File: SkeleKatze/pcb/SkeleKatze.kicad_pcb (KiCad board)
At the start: 2 copper layers, 54.5 x 82.9 mm, 6 parts, among them SW2 SW_Push

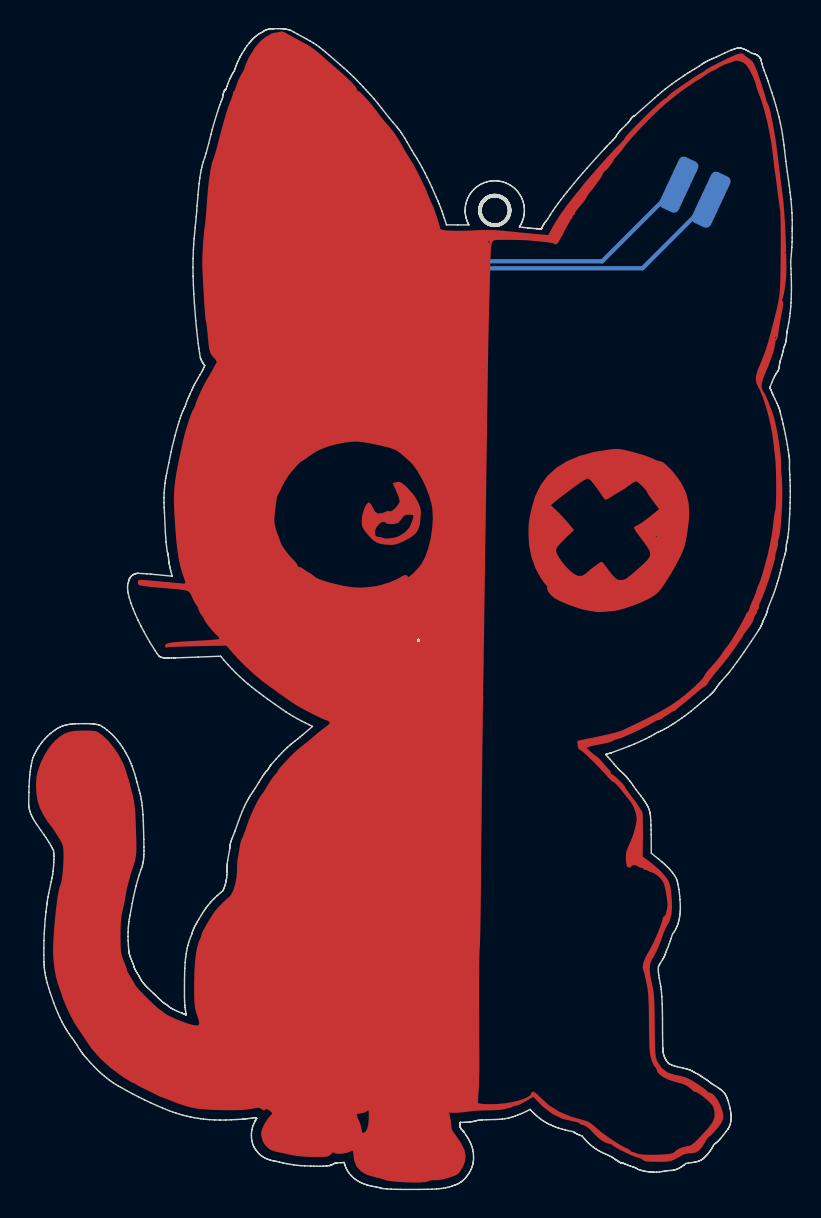
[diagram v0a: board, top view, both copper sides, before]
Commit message: Updated base image to fix mask issues
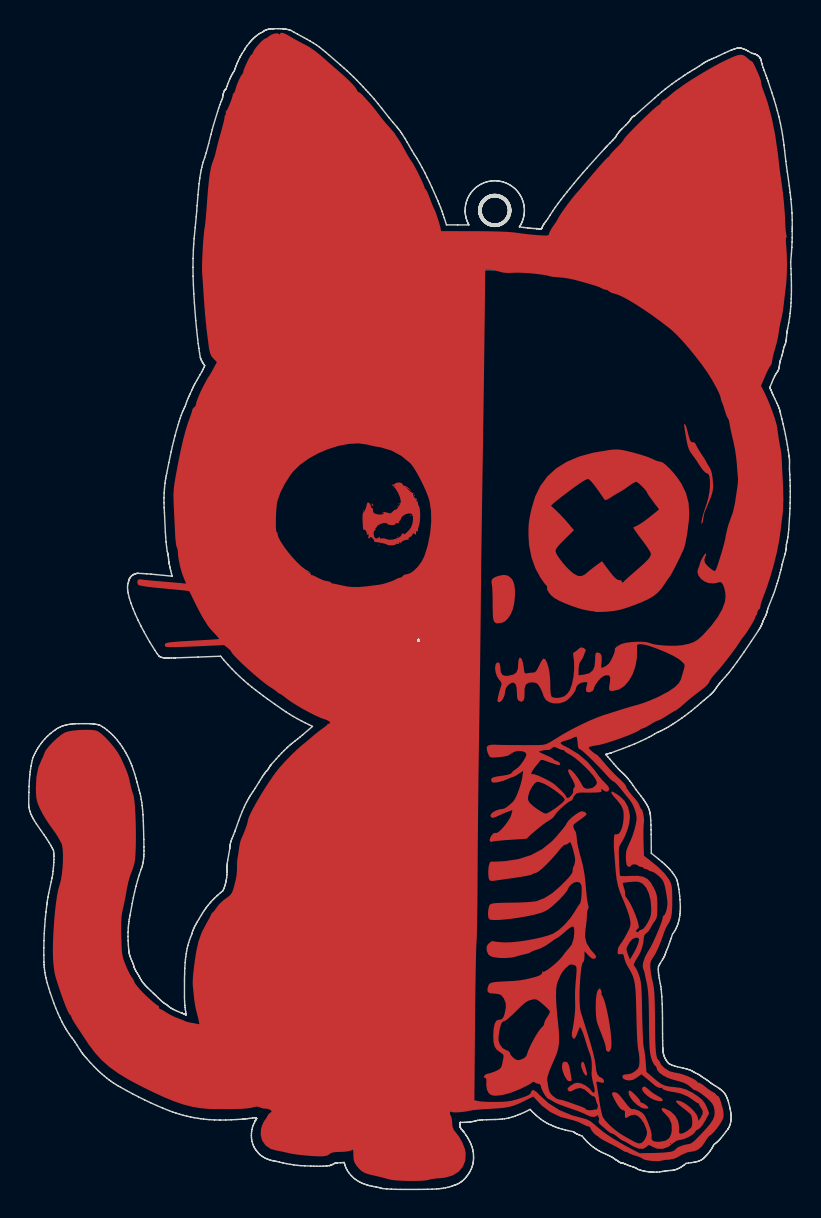
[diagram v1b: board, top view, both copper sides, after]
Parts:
- Lg1: footprint SkeleKatze-Lib:SkeleKatze-Merged-NFS -> SkeleKatze-Lib:SkeleKatze-R2.0
- moved Lg2 0.31 mm to (207.2, 43.9)
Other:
- board text added: "Schrödingers Katze David Füleki R${REVISION} Steve Mayze"
- board text removed: "Schrödingers Katze David Füleki R1.0"
